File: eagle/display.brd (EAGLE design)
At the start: 17.8 x 45.7 mm, 40 parts, among them IC5 APX803, P1IN TPTP10R, P1RET TPTP10R, P2IN TPTP10R, P2RET TPTP10R, P3IN TPTP10R, P3RET TPTP10R, P4IN TPTP10R, Q1 MMBT2222, T1 BC846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

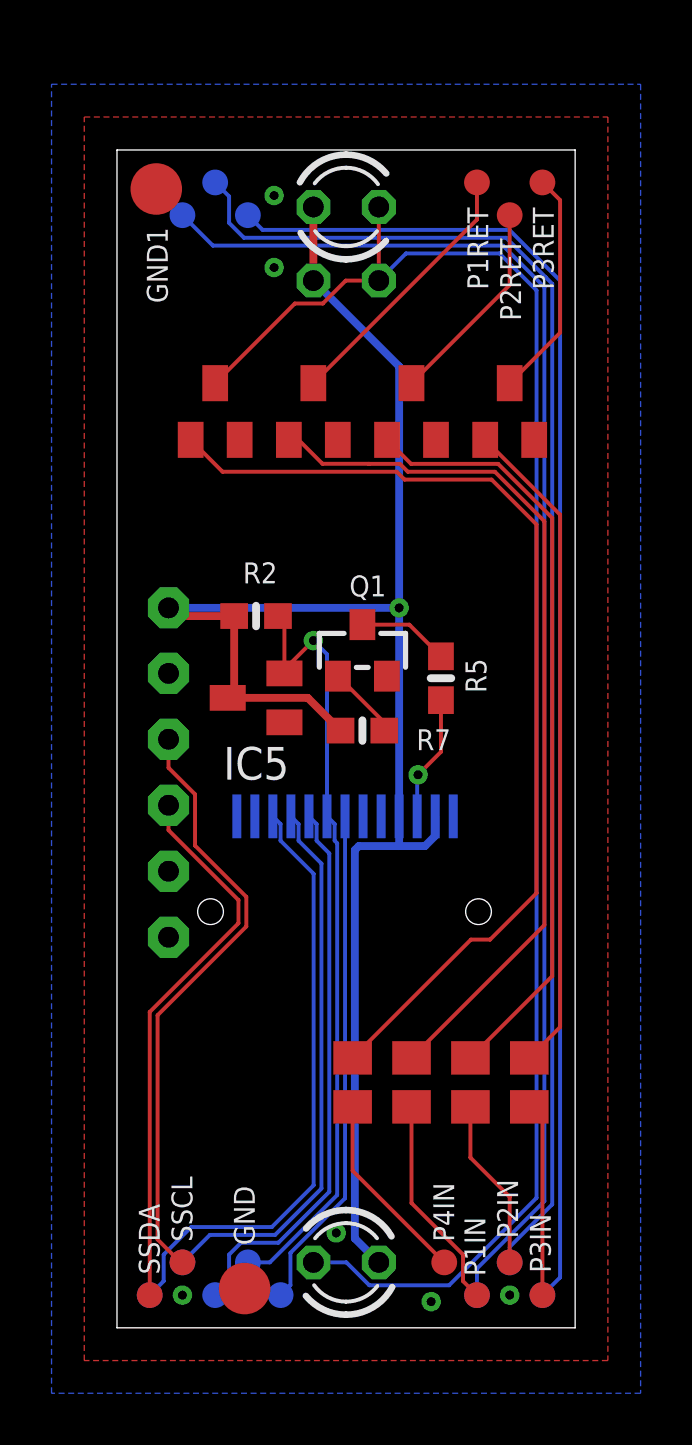
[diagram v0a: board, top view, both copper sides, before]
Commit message: Display board redesigned with FFC connector
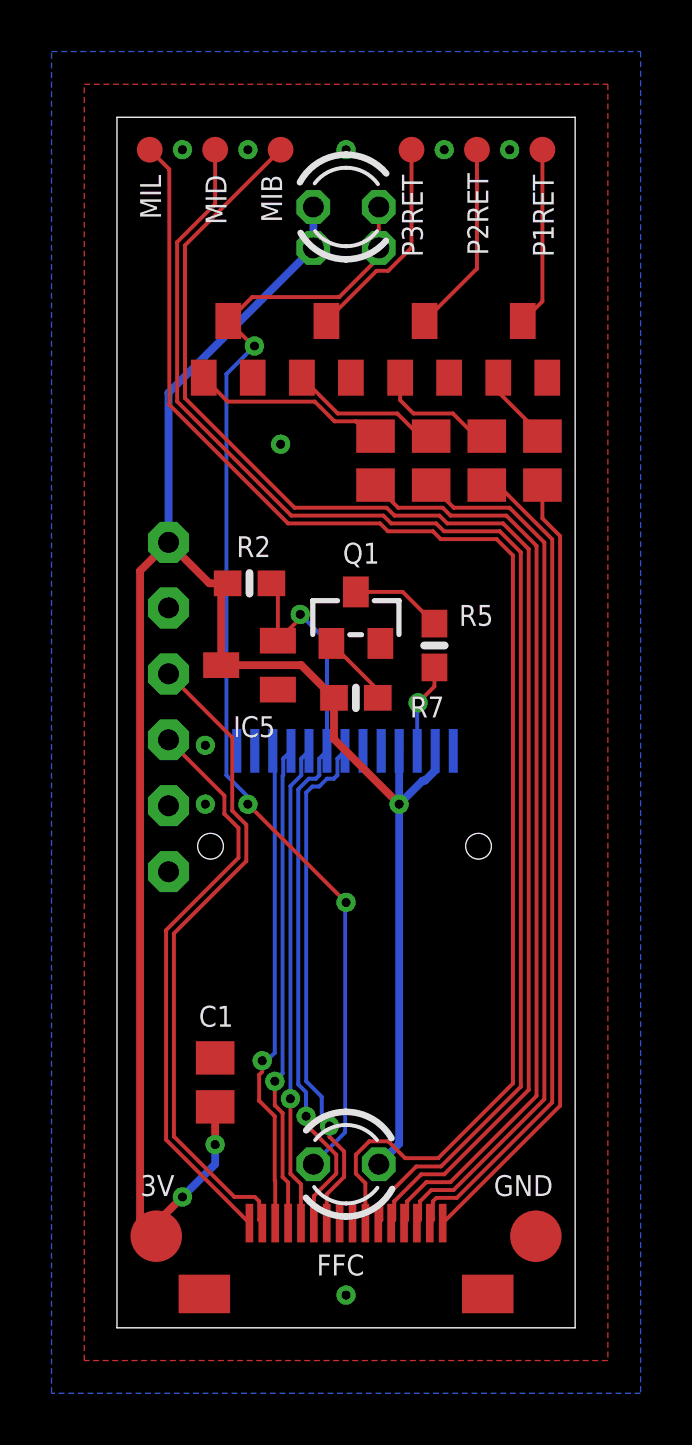
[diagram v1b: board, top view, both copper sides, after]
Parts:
- removed DC, MIB1, MID1, MIL1, MOSI, P1IN, P2IN, P3IN, P4IN, SCK, SSCL, SSDA, TFTCS, TFTRST: TPTP10R, testpad:TP10R
- removed GND1: TPTP20R, testpad:TP20R
- added 3V: TPTP20R, testpad:TP20R
- added C1: (no value), resistor:C0805
- added U$3: 16PINFFC, general:16PINFFC
- moved MIL 47.0 mm to (1.27, 45.7), flipped to the top
- moved MIB 45.1 mm to (6.35, 45.7), flipped to the top
- moved MID 44.7 mm to (3.81, 45.7), flipped to the top
- moved R1 24.7 mm to (16.5, 33.7)
- moved R4 24.4 mm to (12.2, 33.7)
- moved R6 24.1 mm to (10.0, 33.7)
- moved R3 24.1 mm to (14.4, 33.7)
- moved GND 11.5 mm to (16.3, 3.56)
- moved T1 8.48 mm to (15.7, 38.0)
- moved T3 7.51 mm to (8.13, 38.0)
- moved P3RET 5.24 mm to (11.4, 45.7)
- moved LED3 3.81 mm to (8.89, 6.35)
- moved P1RET 2.84 mm to (16.5, 45.7)
- moved P2RET 2.84 mm to (14.0, 45.7)
- moved DISP1 2.54 mm to (8.89, 8.89)
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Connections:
- removed net N$11: P1IN.TP, R1.1
- removed net N$12: P2IN.TP, R3.1
- removed net N$13: P3IN.TP, R4.1
- removed net N$16: P4IN.TP, R6.1
- removed net N$2: SSCL.TP, U$2.SPECSEL
- removed net N$3: SSDA.TP, U$2.SPECSDA
- new net P1IN: R1.1, U$3.1
- new net P2IN: R3.1, U$3.2
- new net P3IN: R4.1, U$3.3
- new net P4IN: R6.1, U$3.4
- new net SSCL: U$2.SPECSEL, U$3.15
- new net SSDA: U$2.SPECSDA, U$3.16
- net 3V: now also 3V.TP, C1.2
- net BCLK: now also U$3.5; no longer MIB1.TP
- net DC: now also U$3.12; no longer DC.TP
- net DOUT: now also U$3.6; no longer MID1.TP
- net GND: now also C1.1, U$3.8, U$3.9, U$3.BASE1, U$3.BASE2; no longer GND1.TP
- net LRCL: now also U$3.7; no longer MIL1.TP
- net MOSI: now also U$3.14; no longer MOSI.TP
- net SCK: now also U$3.13; no longer SCK.TP
- net TFTCS: now also U$3.10; no longer TFTCS.TP
- net TFTRST: now also U$3.11; no longer TFTRST.TP
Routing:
- net P4IN: track 0.00 -> 36.2 mm
- net P3IN: track 0.00 -> 34.3 mm
- net P2IN: track 0.00 -> 32.4 mm
- net N$14: track 38.9 -> 7.60 mm
- net N$4: track 34.2 -> 2.98 mm
- net P1IN: track 0.00 -> 30.8 mm
- net SSCL: track 0.00 -> 25.6 mm
- net N$6: track 29.9 -> 4.81 mm
- net N$2: track 23.4 -> 0.00 mm
- net SSDA: track 0.00 -> 22.4 mm
- net N$3: track 21.6 -> 0.00 mm
- net N$7: track 25.7 -> 5.95 mm
- net PWM4: track 63.7 -> 44.9 mm, vias 0 -> 3
- net 3V: track 66.5 -> 84.3 mm, vias 1 -> 3
- net N$11: track 8.36 -> 0.00 mm
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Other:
- board size 17.8 x 45.7 mm -> 17.8 x 47 mm
- board text added: "FFC"
